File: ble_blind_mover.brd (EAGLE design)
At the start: 56 x 73.8 mm, 47 parts, among them Q2 DMG6968U-7, T1 BT138-V, U1 MCP7940N-I/SN, U2 YJ-14015, U3 IRM-01-5, U4 MIC5205-3.3YM5-TR, Y1 LFXTAL016178

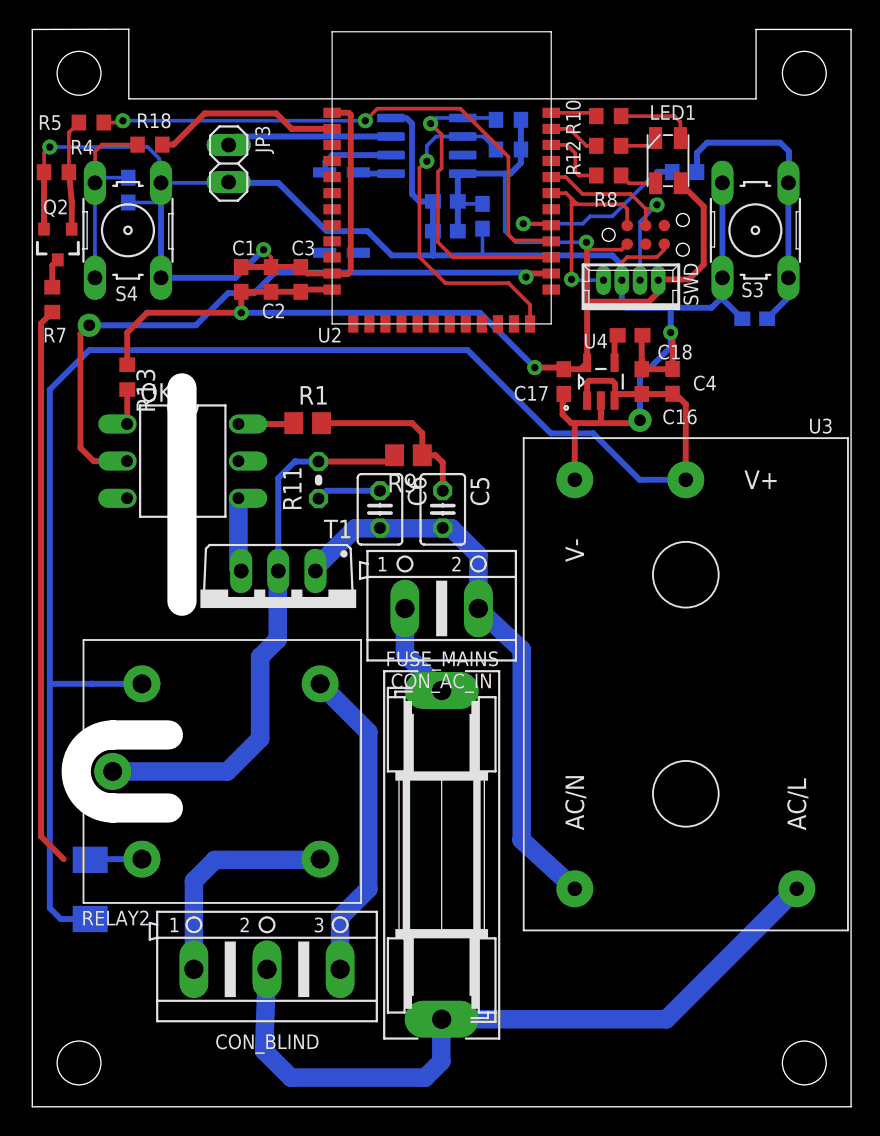
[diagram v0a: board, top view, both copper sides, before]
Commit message: Added B2B connector for I2C
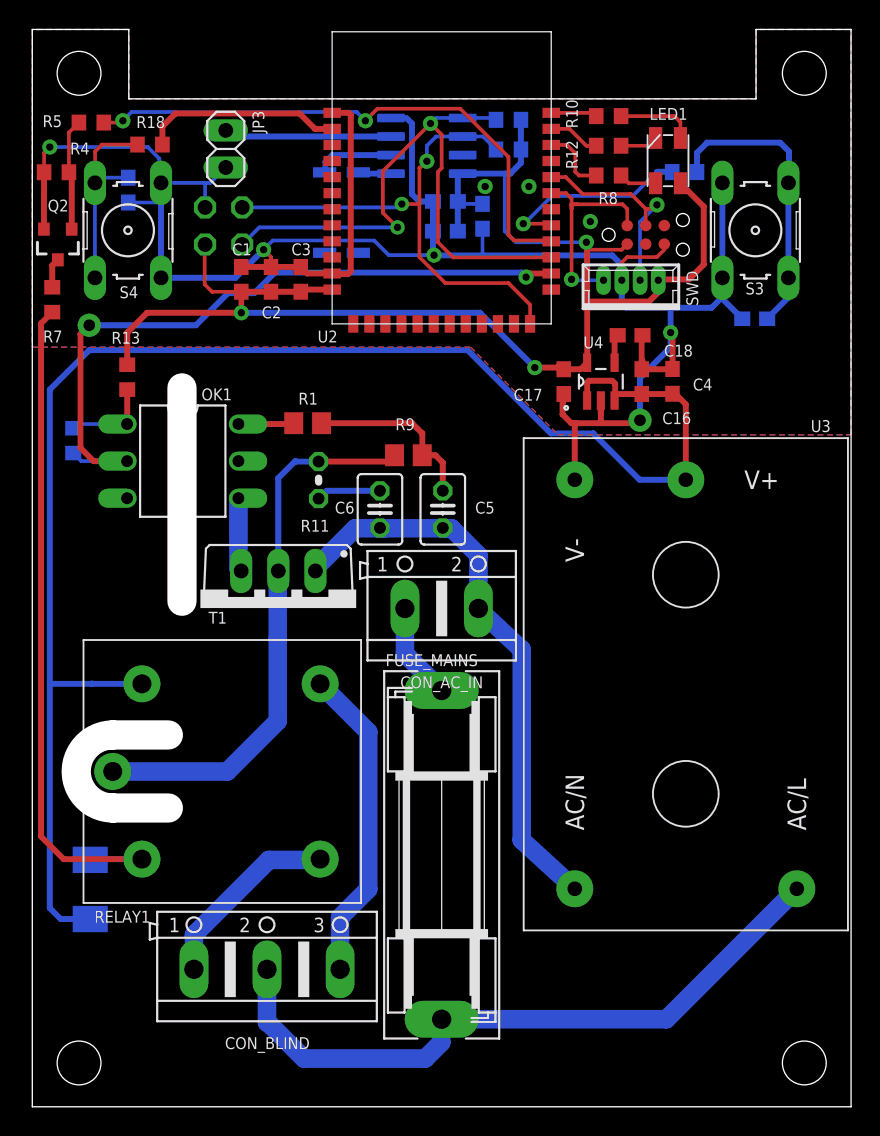
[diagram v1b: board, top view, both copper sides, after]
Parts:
- added JP1: (no value), pinhead:2X02
- added R2: TBD, rcl:R0603
- moved JP3 1.02 mm to (13.2, 65.6)
- renumbered RELAY2 to RELAY1
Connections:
- net +3V3: now also JP1.4
- net ENABLE: now also R2.2
- net GND: now also JP1.2
- net MOC_AN: now also R2.1
- net SCL: now also JP1.1
- net SDA: now also JP1.3
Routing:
- net SDA: track 21.4 -> 41.4 mm, vias 1 -> 2
- net SCL: track 23.5 -> 35.7 mm, vias 1 -> 2
- net +3V3: track 97.2 -> 102.6 mm
- net RELAY_COIL_DIR: track 42.0 -> 47.3 mm
- net ENABLE: track 45.6 -> 49.5 mm
- net MOC_AN: track 2.36 -> 6.17 mm
- net LINE_FUSED: track 49.8 -> 46.7 mm
- net BLIND_UP_AC: track 15.3 -> 13.1 mm
- net GND: track 156.3 -> 154.6 mm, vias 4 -> 8
- net BTN_DOWN: track 12.9 -> 13.7 mm
- added copper zone on layer 1, net GND
- added copper zone on layer 16, net GND
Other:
- outline, holes or cut-outs redrawn
